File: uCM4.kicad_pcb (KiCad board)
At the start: 2 copper layers, 55 x 40 mm, 30 parts, among them J1 Conn_01x03, J2 Ethernet, J3 Micro_SD_Card, J4 USB_B_Micro, SW1 SW_DIP_x01, SW2 SW_DIP_x01, U1 RT9742GGJ5, U2 74LVC1G07, U3 TPD4EUSB30

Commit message: Even more routing
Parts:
- moved C2 11.1 mm to (170.0, 83.0), turned to 90 degrees
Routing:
- net Net-(C2-Pad1): track 0.00 -> 6.08 mm
- net /Eth_P0_P: track 4.17 -> 0.00 mm
- net Net-(Module1-Pad21): track 41.1 -> 41.4 mm, vias 3 -> 1

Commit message: Configure DP router
Reconfigure board rules to allow routing differential pairs.
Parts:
- moved R3 3.77 mm to (167.0, 94.5)
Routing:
- net Net-(Module1-Pad95): track 45.7 -> 39.5 mm
- net Net-(Module1-Pad20): track 2.84 -> 0.00 mm, vias 1 -> 0
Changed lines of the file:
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@@
     (pad "" np_thru_hole circle (at -5.715 0 90) (locked) (size 3.25 3.25) (drill 3.25) (layers F&B.Cu *.Mask))
     (pad "L1" thru_hole circle (at 6.63 4.06 90) (locked) (size 1.524 1.524) (drill 0.9) (layers *.Cu *.Mask)
-      (net 10 "+3V3") (pinfunction "Y+"))
+      (net 10 "+3V3") (pinfunction "Y+") (pintype "bidirectional"))
     (pad "L2" thru_hole circle (at 4.09 4.06 90) (locked) (size 1.524 1.524) (drill 0.9) (layers *.Cu *.Mask)
-      (net 121 "Net-(R12-Pad1)") (pinfunction "Y-"))
+      (net 121 "Net-(R12-Pad1)") (pinfunction "Y-") (pintype "bidirectional"))
     (pad "L3" thru_hole circle (at -4.09 4.06 90) (locked) (size 1.524 1.524) (drill 0.9) (layers *.Cu *.Mask)
-      (net 119 "Net-(R14-Pad1)") (pinfunction "G-"))
+      (net 119 "Net-(R14-Pad1)") (pinfunction "G-") (pintype "bidirectional"))
     (pad "L4" thru_hole circle (at -6.63 4.06 90) (locked) (size 1.524 1.524) (drill 0.9) (layers *.Cu *.Mask)
-      (net 10 "+3V3") (pinfunction "G+"))
+      (net 10 "+3V3") (pinfunction "G+") (pintype "bidirectional"))
     (pad "R1" thru_hole circle (at -5.715 -8.89 90) (locked) (size 1.524 1.524) (drill 1) (layers *.Cu *.Mask)
-      (net 115 "/Eth_P0_P") (pinfunction "TD1+"))
+      (net 115 "/Eth_P0_P") (pinfunction "TD1+") (pintype "bidirectional"))
     (pad "R2" thru_hole circle (at -4.445 -6.35 90) (locked) (size 1.524 1.524) (drill 1) (layers *.Cu *.Mask)
-      (net 111 "/Eth_P0_N") (pinfunction "TD1-"))
+      (net 111 "/Eth_P0_N") (pinfunction "TD1-") (pintype "bidirectional"))
     (pad "R3" thru_hole circle (at -3.175 -8.87 90) (locked) (size 1.524 1.524) (drill 1) (layers *.Cu *.Mask)
-      (net 70 "/Eth_P1_P") (pinfunction "TD2+"))
+      (net 70 "/Eth_P1_P") (pinfunction "TD2+") (pintype "bidirectional"))
     (pad "R4" thru_hole circle (at -1.905 -6.35 90) (locked) (size 1.524 1.524) (drill 1) (layers *.Cu *.Mask)
-      (net 69 "/Eth_P1_N") (pinfunction "TD2-"))
+      (net 69 "/Eth_P1_N") (pinfunction "TD2-") (pintype "bidirectional"))
     (pad "R5" thru_hole circle (at -0.635 -8.87 90) (locked) (size 1.524 1.524) (drill 1) (layers *.Cu *.Mask)
-      (net 9 "Net-(C2-Pad1)") (pinfunction "CT"))
+      (net 9 "Net-(C2-Pad1)") (pinfunction "CT") (pintype "bidirectional"))
     (pad "R6" thru_hole circle (at 0.635 -6.35 90) (locked) (size 1.524 1.524) (drill 1) (layers *.Cu *.Mask)
-      (net 9 "Net-(C2-Pad1)") (pinfunction "CT"))
+      (net 9 "Net-(C2-Pad1)") (pinfunction "CT") (pintype "bidirectional"))
     (pad "R7" thru_hole circle (at 1.905 -8.87 90) (locked) (size 1.524 1.524) (drill 1) (layers *.Cu *.Mask)
-      (net 64 "/Eth_P2_P") (pinfunction "TD3+"))
+      (net 64 "/Eth_P2_P") (pinfunction "TD3+") (pintype "bidirectional"))
     (pad "R8" thru_hole circle (at 3.175 -6.35 90) (locked) (size 1.524 1.524) (drill 1) (layers *.Cu *.Mask)
-      (net 63 "/Eth_P2_N") (pinfunction "TD3-"))
+      (net 63 "/Eth_P2_N") (pinfunction "TD3-") (pintype "bidirectional"))
     (pad "R9" thru_hole circle (at 4.445 -8.87 90) (locked) (size 1.524 1.524) (drill 1) (layers *.Cu *.Mask)
-      (net 57 "/Eth_P3_P") (pinfunction "TD4+"))
+      (net 57 "/Eth_P3_P") (pinfunction "TD4+") (pintype "bidirectional"))
     (pad "R10" thru_hole circle (at 5.715 -6.35 90) (locked) (size 1.524 1.524) (drill 1) (layers *.Cu *.Mask)
-      (net 51 "/Eth_P3_N") (pinfunction "TD4-"))
+      (net 51 "/Eth_P3_N") (pinfunction "TD4-") (pintype "bidirectional"))
     (pad "Shield" thru_hole circle (at -7.775 -3.05 90) (size 2 2) (drill 1.5) (layers *.Cu *.Mask))
     (pad "Shield" thru_hole circle (at 7.775 -3.05 90) (size 2 2) (drill 1.5) (layers *.Cu *.Mask))
@@
   )
   (footprint "Resistor_SMD:R_0603_1608Metric_Pad0.98x0.95mm_HandSolder" (layer "F.Cu")
-    (at 170.75 94.0875 -90)
+    (at 167 94.5 -90)
     (descr "Resistor SMD 0603 (1608 Metric), square (rectangular) end terminal, IPC_7351 nominal with elongated pad for handsoldering. (Body size source: IPC-SM-782 page 72, https://www.pcb-3d.com/wordpress/wp-content/uploads/ipc-sm-782a_amendment_1_and_2.pdf), generated with kicad-footprint-generator")
     (tags "resistor handsolder")
@@
   (segment (start 169.5 98.915) (end 169.423989 98.991011) (width 0.13) (layer "B.Cu") (net 76))
   (segment (start 169.423989 98.991011) (end 169.423989 99.715011) (width 0.13) (layer "B.Cu") (net 76))
-  (segment (start 170.75 95) (end 170 95) (width 0.13) (layer "F.Cu") (net 81))
-  (segment (start 170 95) (end 169.5 95.5) (width 0.13) (layer "F.Cu") (net 81))
-  (via (at 169.5 95.5) (size 0.45) (drill 0.25) (layers "F.Cu" "B.Cu") (net 81))
-  (segment (start 169.5 95.5) (end 168.989 96.011) (width 0.13) (layer "B.Cu") (net 81))
-  (segment (start 168.989 96.011) (end 168.989 96.67) (width 0.13) (layer "B.Cu") (net 81))
   (segment (start 169.50252 94.24748) (end 171.75252 94.24748) (width 0.13) (layer "F.Cu") (net 82))
   (segment (start 174.522989 91.029511) (end 174.522989 90.977011) (width 0.13) (layer "F.Cu") (net 82))
@@
   (segment (start 155 96.659) (end 154.989 96.67) (width 0.13) (layer "B.Cu") (net 108))
   (segment (start 155 95.75) (end 155 96.281) (width 0.13) (layer "B.Cu") (net 108))
-  (segment (start 156.627771 80.750012) (end 162.86066 80.750012) (width 0.13) (layer "F.Cu") (net 113))
   (segment (start 172.5 71.110672) (end 172.5 69.25) (width 0.13) (layer "F.Cu") (net 113))
   (segment (start 152 85.377783) (end 156.627771 80.750012) (width 0.13) (layer "F.Cu") (net 113))

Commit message: Route first pair and adjust length
Has to be done in two steps:
1. Draw differential pair.
2. Adjust length of differential pair tracks.
3. Repeat (2) until net inspector shows they are even.
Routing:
- net /Eth_P0_P: track 0.00 -> 11.0 mm
- net /Eth_P0_N: track 0.00 -> 11.0 mm
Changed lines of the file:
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@@
   (segment (start 155 96.659) (end 154.989 96.67) (width 0.13) (layer "B.Cu") (net 108))
   (segment (start 155 95.75) (end 155 96.281) (width 0.13) (layer "B.Cu") (net 108))
+  (segment (start 173.324489 89.880511) (end 173.468646 89.880511) (width 0.127) (layer "B.Cu") (net 111))
+  (segment (start 170.9175 92.2875) (end 173.324489 89.880511) (width 0.127) (layer "B.Cu") (net 111))
+  (segment (start 173.965511 89.383646) (end 173.965511 89.239489) (width 0.127) (layer "B.Cu") (net 111))
+  (segment (start 173.965511 89.239489) (end 175.55 87.655) (width 0.127) (layer "B.Cu") (net 111))
+  (segment (start 170.9175 96.073499) (end 170.9175 92.2875) (width 0.127) (layer "B.Cu") (net 111))
+  (segment (start 173.468646 89.880511) (end 173.965511 89.383646) (width 0.127) (layer "B.Cu") (net 111))
+  (segment (start 170.989 96.144999) (end 170.9175 96.073499) (width 0.127) (layer "B.Cu") (net 111))
+  (segment (start 170.989 96.67) (end 170.989 96.144999) (width 0.127) (layer "B.Cu") (net 111))
   (segment (start 172.5 71.110672) (end 172.5 69.25) (width 0.13) (layer "F.Cu") (net 113))
   (segment (start 152 85.377783) (end 156.627771 80.750012) (width 0.13) (layer "F.Cu") (net 113))
@@
   (segment (start 153.789 99.75) (end 153.789 99.22298) (width 0.13) (layer "B.Cu") (net 113))
   (segment (start 148 89.25) (end 154.5 89.25) (width 0.13) (layer "B.Cu") (net 114))
+  (segment (start 170.3605 93.081047) (end 170.427256 93.088568) (width 0.127) (layer "B.Cu") (net 115))
+  (segment (start 170.29144 93.081047) (end 170.3605 93.081047) (width 0.127) (layer "B.Cu") (net 115))
+  (segment (start 171.341924 90.096045) (end 171.289402 90.13793) (width 0.127) (layer "B.Cu") (net 115))
+  (segment (start 170.224683 93.073525) (end 170.29144 93.081047) (width 0.127) (layer "B.Cu") (net 115))
+  (segment (start 170.589 96.144999) (end 170.589 96.67) (width 0.127) (layer "B.Cu") (net 115))
+  (segment (start 171.535123 90.051948) (end 171.467944 90.051948) (width 0.127) (layer "B.Cu") (net 115))
+  (segment (start 171.996509 90.420773) (end 171.713666 90.13793) (width 0.127) (layer "B.Cu") (net 115))
+  (segment (start 170.29144 92.481047) (end 170.224683 92.488568) (width 0.127) (layer "B.Cu") (net 115))
+  (segment (start 170.427256 93.088568) (end 170.490665 93.110756) (width 0.127) (layer "B.Cu") (net 115))
+  (segment (start 171.572244 90.845036) (end 171.614129 90.897559) (width 0.127) (layer "B.Cu") (net 115))
+  (segment (start 170.161274 93.051337) (end 170.224683 93.073525) (width 0.127) (layer "B.Cu") (net 115))
+  (segment (start 170.490665 93.110756) (end 170.547546 93.146497) (width 0.127) (layer "B.Cu") (net 115))
+  (segment (start 171.658226 91.090758) (end 171.643277 91.156252) (width 0.127) (layer "B.Cu") (net 115))
+  (segment (start 171.661143 90.096045) (end 171.600617 90.066897) (width 0.127) (layer "B.Cu") (net 115))
+  (segment (start 171.572245 91.269301) (end 171.185418 91.656129) (width 0.127) (layer "B.Cu") (net 115))
+  (segment (start 170.6605 93.381047) (end 170.6605 96.073499) (width 0.127) (layer "B.Cu") (net 115))
+  (segment (start 171.247516 90.190452) (end 171.218369 90.250978) (width 0.127) (layer "B.Cu") (net 115))
+  (segment (start 171.658226 91.023579) (end 171.658226 91.090758) (width 0.127) (layer "B.Cu") (net 115))
+  (segment (start 172.175052 90.506754) (end 172.109558 90.491805) (width 0.127) (layer "B.Cu") (net 115))
+  (segment (start 171.185418 91.656129) (end 170.6605 92.181047) (width 0.127) (layer "B.Cu") (net 115))
+  (segment (start 170.3605 92.481047) (end 170.29144 92.481047) (width 0.127) (layer "B.Cu") (net 115))
+  (segment (start 171.713666 90.13793) (end 171.661143 90.096045) (width 0.127) (layer "B.Cu") (net 115))
+  (segment (start 171.643277 91.156252) (end 171.614129 91.216778) (width 0.127) (layer "B.Cu") (net 115))
+  (segment (start 169.998961 92.847803) (end 170.021149 92.911212) (width 0.127) (layer "B.Cu") (net 115))
+  (segment (start 171.20342 90.383651) (end 171.218369 90.449145) (width 0.127) (layer "B.Cu") (net 115))
+  (segment (start 171.218369 90.449145) (end 171.247516 90.509671) (width 0.127) (layer "B.Cu") (net 115))
+  (segment (start 171.614129 90.897559) (end 171.643277 90.958085) (width 0.127) (layer "B.Cu") (net 115))
+  (segment (start 171.40245 90.066897) (end 171.341924 90.096045) (width 0.127) (layer "B.Cu") (net 115))
+  (segment (start 170.547546 92.415596) (end 170.490665 92.451337) (width 0.127) (layer "B.Cu") (net 115))
+  (segment (start 170.05689 92.594) (end 170.021149 92.650881) (width 0.127) (layer "B.Cu") (net 115))
+  (segment (start 172.242231 90.506754) (end 172.175052 90.506754) (width 0.127) (layer "B.Cu") (net 115))
+  (segment (start 171.247516 90.509671) (end 171.289402 90.562194) (width 0.127) (layer "B.Cu") (net 115))
+  (segment (start 172.307725 90.491805) (end 172.242231 90.506754) (width 0.127) (layer "B.Cu") (net 115))
+  (segment (start 170.652978 92.247803) (end 170.63079 92.311212) (width 0.127) (layer "B.Cu") (net 115))
+  (segment (start 171.289402 90.562194) (end 171.572244 90.845036) (width 0.127) (layer "B.Cu") (net 115))
+  (segment (start 171.614129 91.216778) (end 171.572245 91.269301) (width 0.127) (layer "B.Cu") (net 115))
+  (segment (start 170.224683 92.488568) (end 170.161274 92.510756) (width 0.127) (layer "B.Cu") (net 115))
+  (segment (start 170.63079 92.311212) (end 170.595049 92.368093) (width 0.127) (layer "B.Cu") (net 115))
+  (segment (start 170.6605 96.073499) (end 170.589 96.144999) (width 0.127) (layer "B.Cu") (net 115))
+  (segment (start 173.01 88.925) (end 173.01 89.831547) (width 0.127) (layer "B.Cu") (net 115))
+  (segment (start 172.109558 90.491805) (end 172.049032 90.462658) (width 0.127) (layer "B.Cu") (net 115))
+  (segment (start 173.01 89.831547) (end 172.420774 90.420773) (width 0.127) (layer "B.Cu") (net 115))
+  (segment (start 170.427256 92.473525) (end 170.3605 92.481047) (width 0.127) (layer "B.Cu") (net 115))
+  (segment (start 170.652978 93.31429) (end 170.6605 93.381047) (width 0.127) (layer "B.Cu") (net 115))
+  (segment (start 170.63079 93.250881) (end 170.652978 93.31429) (width 0.127) (layer "B.Cu") (net 115))
+  (segment (start 172.368251 90.462658) (end 172.307725 90.491805) (width 0.127) (layer "B.Cu") (net 115))
+  (segment (start 170.490665 92.451337) (end 170.427256 92.473525) (width 0.127) (layer "B.Cu") (net 115))
+  (segment (start 171.218369 90.250978) (end 171.20342 90.316472) (width 0.127) (layer "B.Cu") (net 115))
+  (segment (start 170.547546 93.146497) (end 170.595049 93.194) (width 0.127) (layer "B.Cu") (net 115))
+  (segment (start 169.998961 92.71429) (end 169.99144 92.781047) (width 0.127) (layer "B.Cu") (net 115))
+  (segment (start 169.99144 92.781047) (end 169.998961 92.847803) (width 0.127) (layer "B.Cu") (net 115))
+  (segment (start 170.6605 92.181047) (end 170.652978 92.247803) (width 0.127) (layer "B.Cu") (net 115))
+  (segment (start 171.467944 90.051948) (end 171.40245 90.066897) (width 0.127) (layer "B.Cu") (net 115))
+  (segment (start 170.595049 92.368093) (end 170.547546 92.415596) (width 0.127) (layer "B.Cu") (net 115))
+  (segment (start 172.049032 90.462658) (end 171.996509 90.420773) (width 0.127) (layer "B.Cu") (net 115))
+  (segment (start 171.643277 90.958085) (end 171.658226 91.023579) (width 0.127) (layer "B.Cu") (net 115))
+  (segment (start 170.161274 92.510756) (end 170.104393 92.546497) (width 0.127) (layer "B.Cu") (net 115))
+  (segment (start 171.600617 90.066897) (end 171.535123 90.051948) (width 0.127) (layer "B.Cu") (net 115))
+  (segment (start 170.05689 92.968093) (end 170.104393 93.015596) (width 0.127) (layer "B.Cu") (net 115))
+  (segment (start 171.20342 90.316472) (end 171.20342 90.383651) (width 0.127) (layer "B.Cu") (net 115))
+  (segment (start 170.021149 92.650881) (end 169.998961 92.71429) (width 0.127) (layer "B.Cu") (net 115))
+  (segment (start 170.021149 92.911212) (end 170.05689 92.968093) (width 0.127) (layer "B.Cu") (net 115))
+  (segment (start 170.595049 93.194) (end 170.63079 93.250881) (width 0.127) (layer "B.Cu") (net 115))
+  (segment (start 170.104393 92.546497) (end 170.05689 92.594) (width 0.127) (layer "B.Cu") (net 115))
+  (segment (start 171.289402 90.13793) (end 171.247516 90.190452) (width 0.127) (layer "B.Cu") (net 115))
+  (segment (start 172.420774 90.420773) (end 172.368251 90.462658) (width 0.127) (layer "B.Cu") (net 115))
+  (segment (start 170.104393 93.015596) (end 170.161274 93.051337) (width 0.127) (layer "B.Cu") (net 115))
   (segment (start 147.875 99.75) (end 150.5 99.75) (width 0.13) (layer "F.Cu") (net 116))
   (via (at 150.5 99.75) (size 0.45) (drill 0.25) (layers "F.Cu" "B.Cu") (net 116))

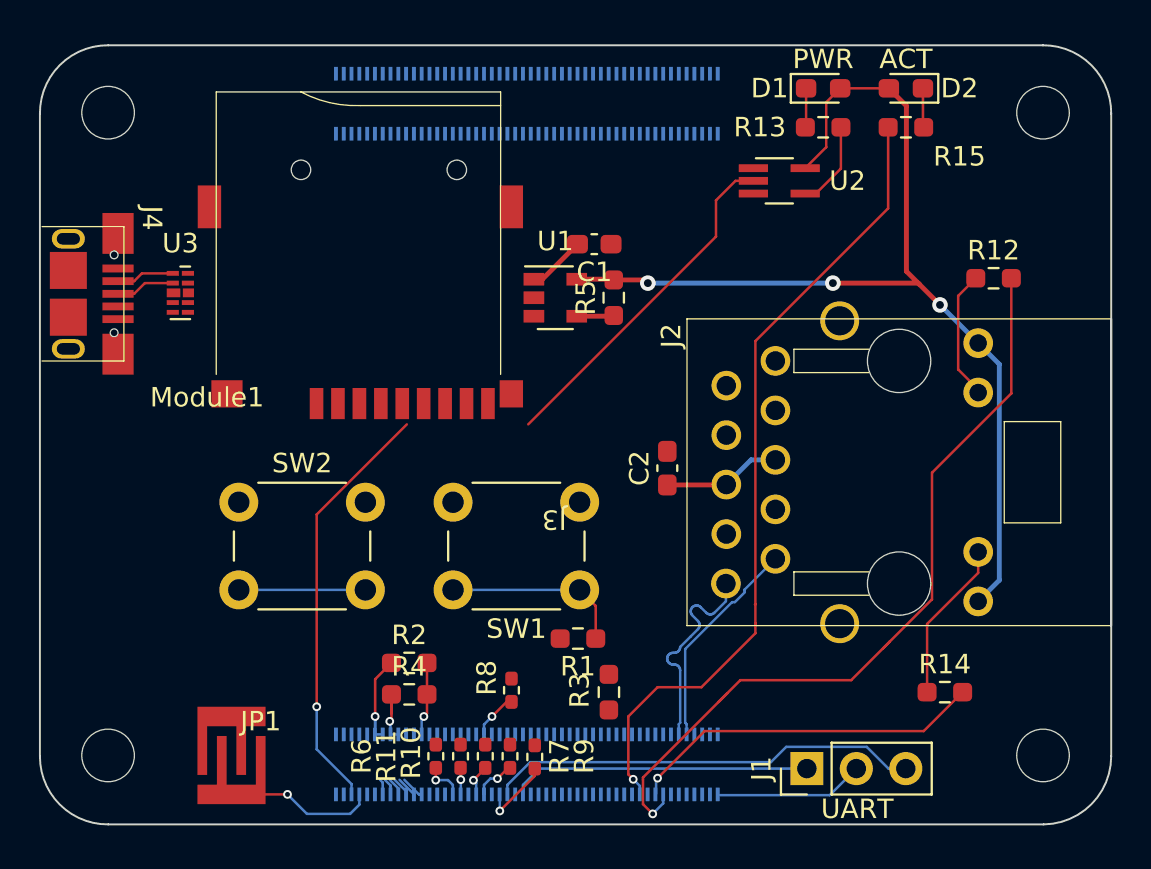
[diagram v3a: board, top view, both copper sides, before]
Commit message: Make USB differential
Rename net to allow differential routing
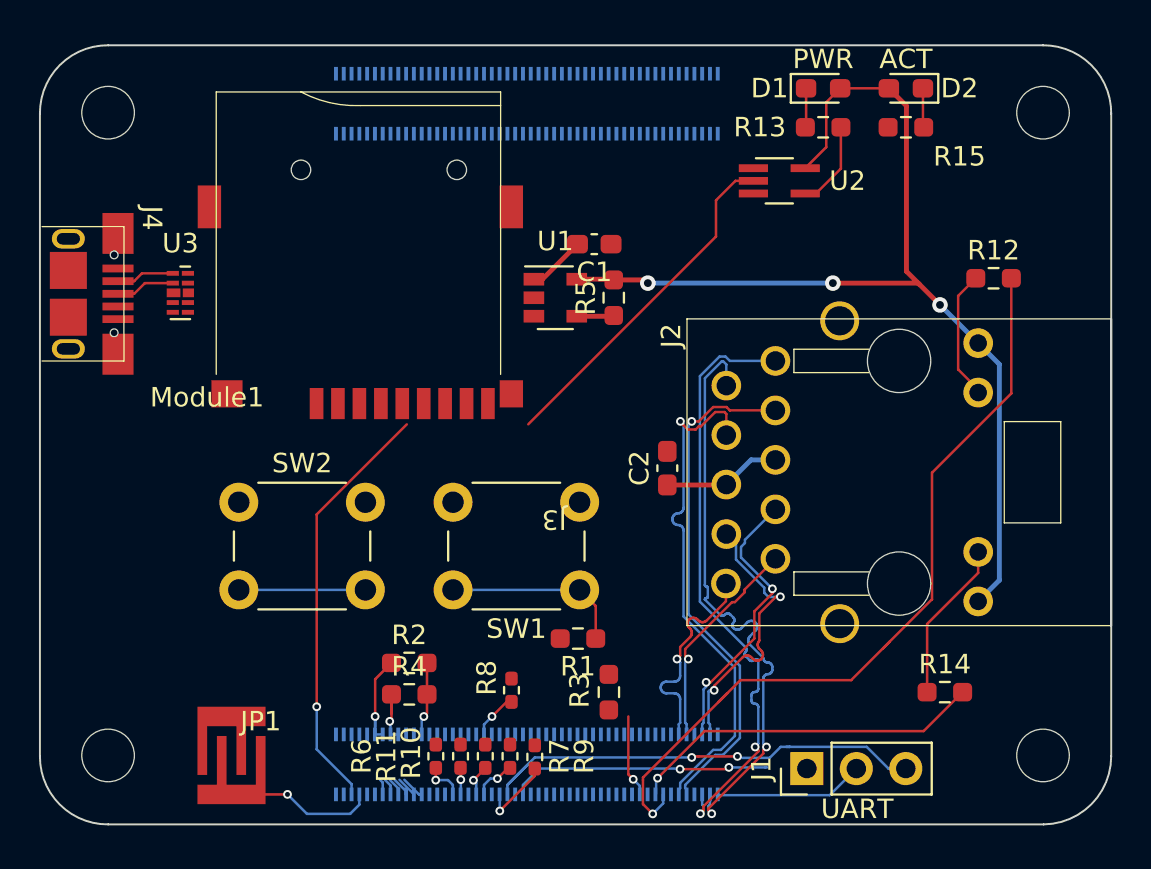
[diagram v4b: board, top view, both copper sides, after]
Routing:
- net Net-(Module1-Pad21): track 41.4 -> 4.24 mm
- net /Eth_P3_N: track 0.00 -> 31.3 mm, vias 0 -> 2
- net /Eth_P3_P: track 0.00 -> 31.3 mm, vias 0 -> 2
- net /Eth_P2_P: track 0.00 -> 26.4 mm, vias 0 -> 1
- net /Eth_P2_N: track 0.00 -> 26.4 mm, vias 0 -> 1
- net /Eth_P1_P: track 0.00 -> 14.6 mm, vias 0 -> 2
- net /Eth_P1_N: track 0.00 -> 14.6 mm, vias 0 -> 2
- net Net-(J1-Pad1): track 15.5 -> 13.5 mm, vias 0 -> 2
- net Net-(J1-Pad3): track 22.3 -> 24.1 mm, vias 0 -> 2
- net /Eth_P0_P: track 11.0 -> 11.2 mm, vias 0 -> 1
- net /Eth_P0_N: track 11.0 -> 11.2 mm, vias 0 -> 1

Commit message: Route USB connection
Not adjusted length yet.
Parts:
- moved U3 0.60 mm to (145.6, 74.0)
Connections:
- net Net-(J4-Pad2) renamed /USB_N
- net Net-(J4-Pad3) renamed /USB_P
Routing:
- net /USB_P: track 3.04 -> 36.2 mm, vias 0 -> 3
- net /USB_N: track 2.98 -> 35.5 mm, vias 0 -> 3
